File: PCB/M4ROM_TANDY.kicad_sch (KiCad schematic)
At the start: 7 parts, among them J1 Tandy_100_102_200_option_rom, J2 4ROM_prog_female, SW1 CUS-14TB, U1 29F010

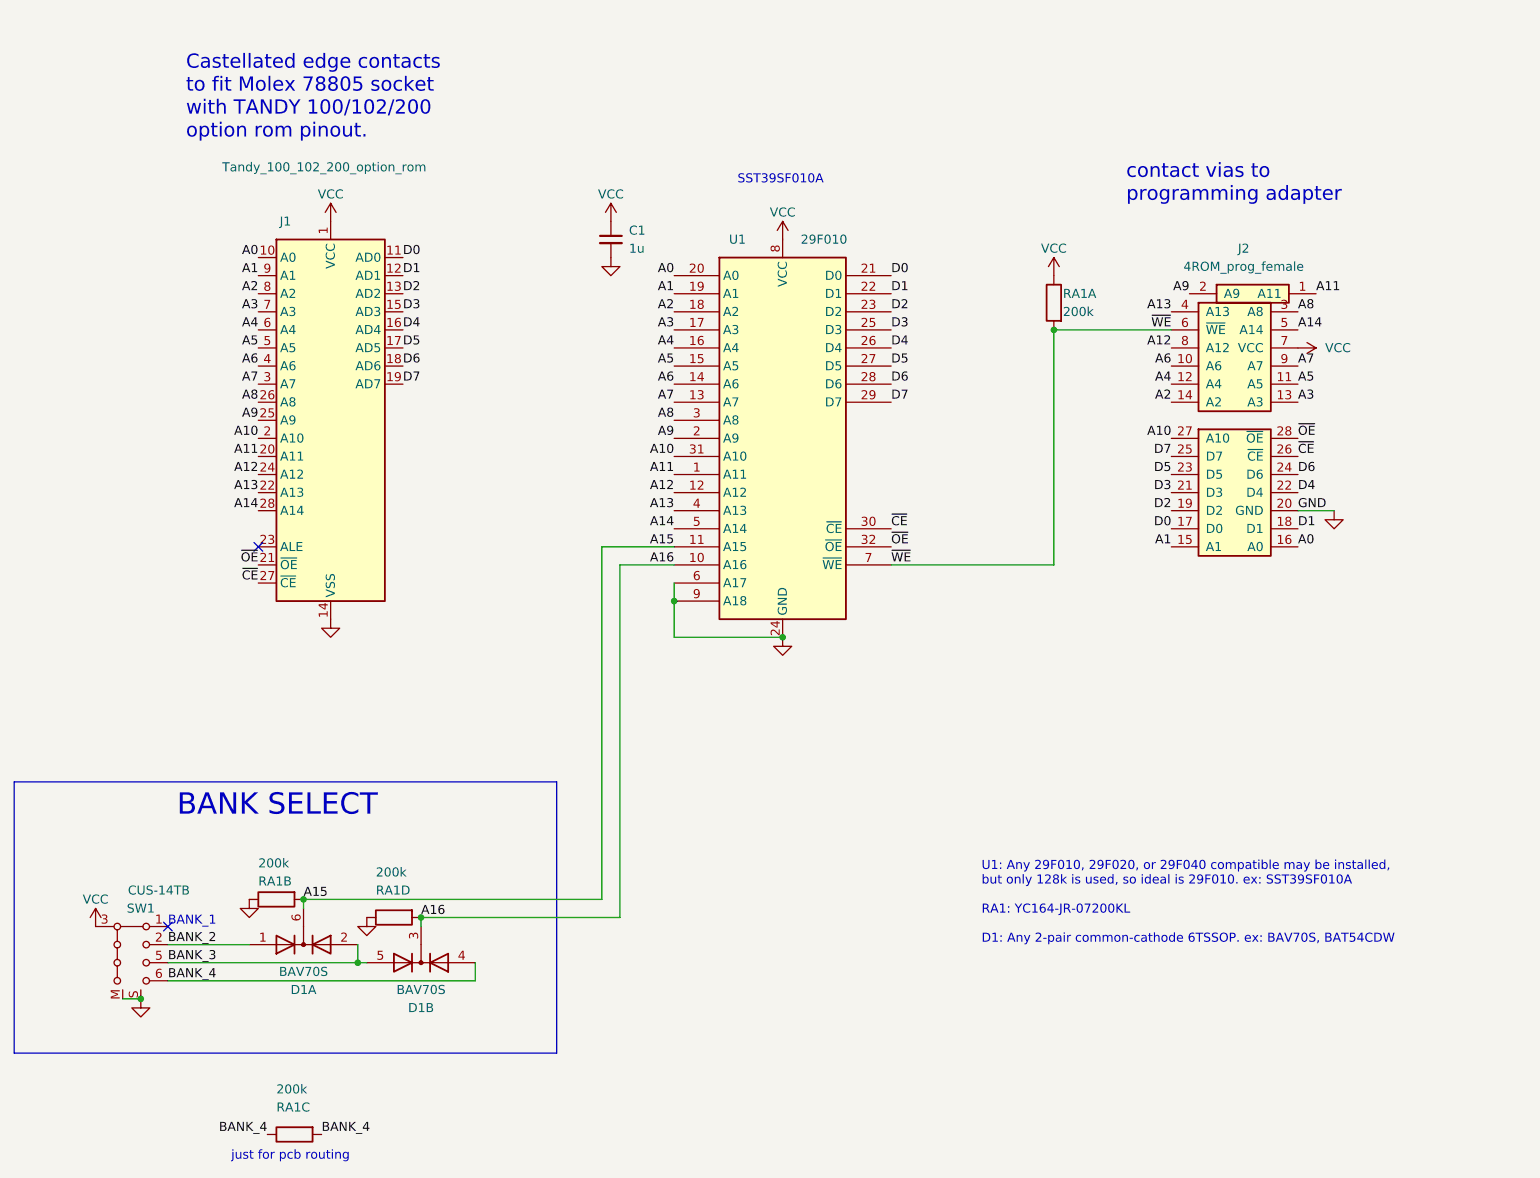
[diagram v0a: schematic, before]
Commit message: MPN boms, centroids, and chip unavailability notes
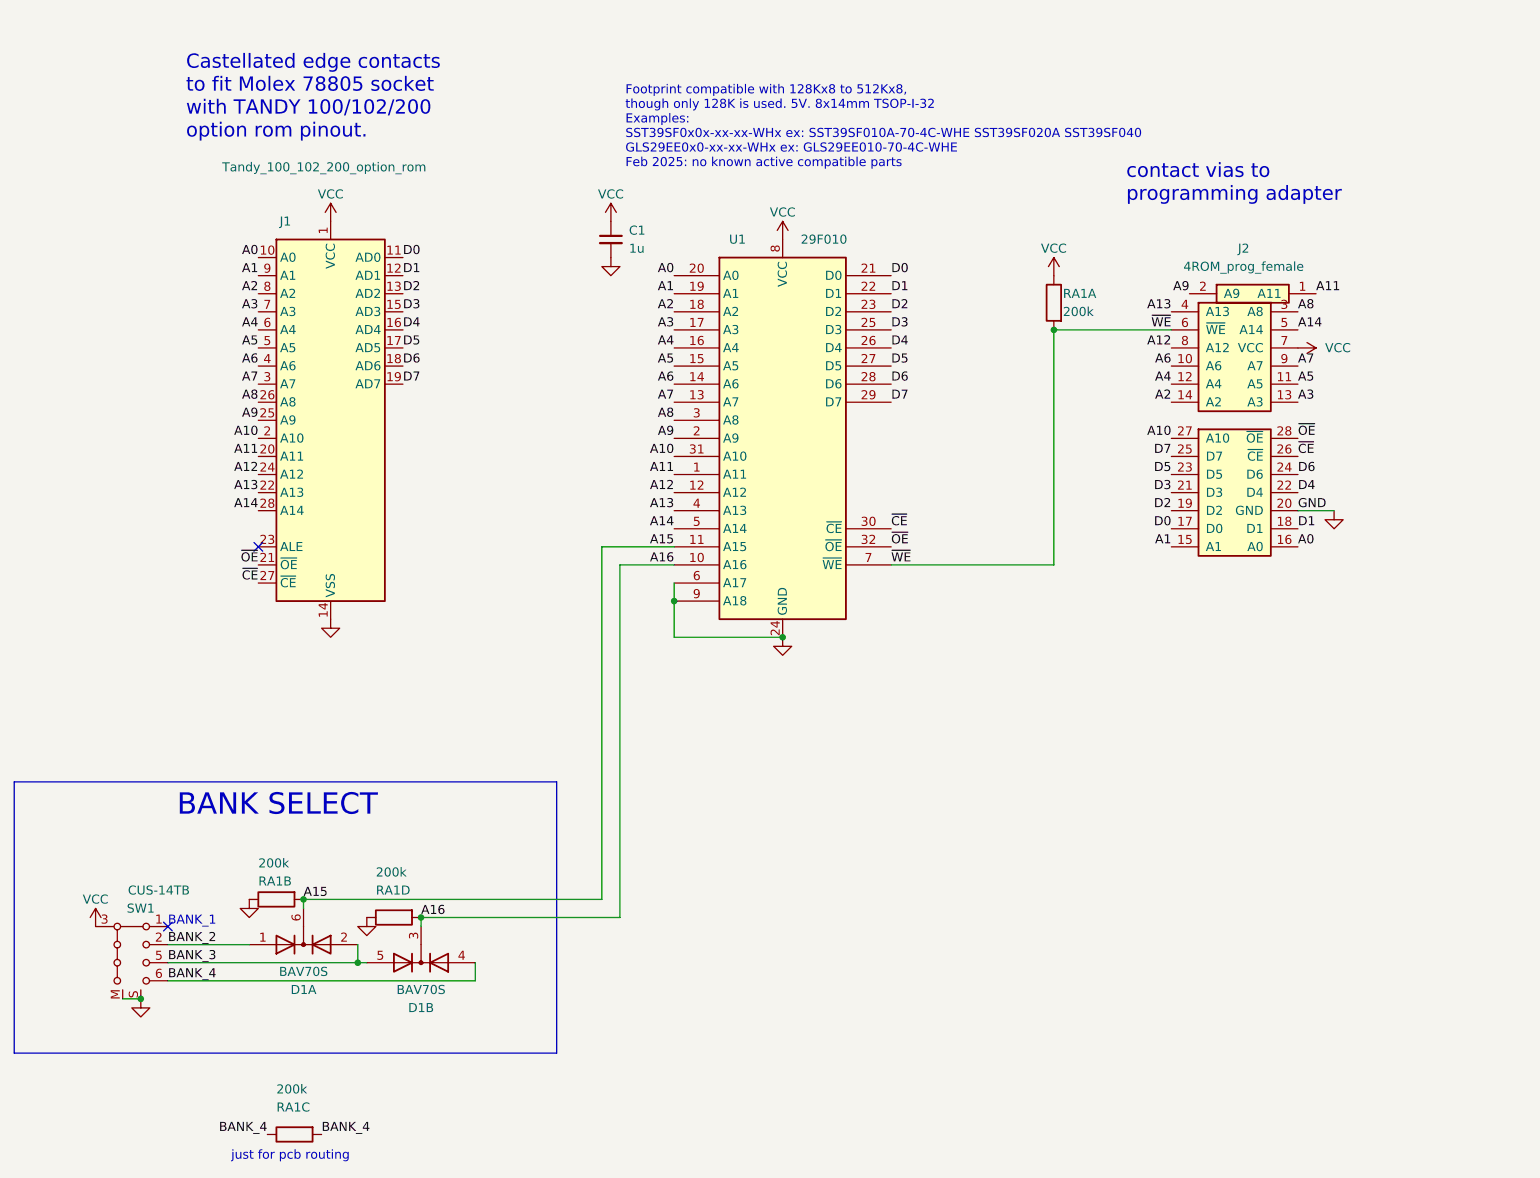
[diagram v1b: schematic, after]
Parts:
- C1: MPN (none) -> CL21B105KBFNNNE
- D1: MPN (none) -> BAV70S,115
- J1, J2: now left out of the parts list
- RA1: MPN (none) -> YC164-JR-07200KL
- SW1: MPN (none) -> CUS-14TB
- U1: MPN (none) -> SST39SF010A-70-4C-WHE
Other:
- note added: "Footprint compatible with 128Kx8 to 512Kx8, though only 128K is used. 5V. 8x14mm TSOP-I-32 Examples: SST39SF0x0x-xx-xx-WHx ex: SST39SF010A-70-4C-WHE SST39SF020A SST39SF040 GLS29EE0x0-xx-xx-WHx ex: GLS29EE010-70-4C-WHE Feb 2025: no known active compatible parts"
- note removed: "SST39SF010A"
- note removed: "U1: Any 29F010, 29F020, or 29F040 compatible may be installed, but only 128k is used, so ideal is 29F010. ex: SST39SF010A RA1: YC164-JR-07200KL D1: Any 2-pair common-cathode 6TSSOP. ex: BAV70S, BAT54CDW"
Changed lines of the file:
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@@
 	(title_block
 		(title "M4ROM TANDY")
-		(date "2023-12-31")
-		(rev "008")
+		(date "2025-02-21")
+		(rev "009")
 		(company "Brian K. White b.kenyon.w@gmail.com")
 		(comment 1 "CC-BY-SA")
@@
 		)
 	)
-	(text "U1: Any 29F010, 29F020, or 29F040 compatible may be installed,\nbut only 128k is used, so ideal is 29F010. ex: SST39SF010A\n\nRA1: YC164-JR-07200KL\n\nD1: Any 2-pair common-cathode 6TSSOP. ex: BAV70S, BAT54CDW\n"
-		(exclude_from_sim no)
-		(at 180.34 162.56 0)
-		(effects
-			(font
-				(size 1.27 1.27)
-			)
-			(justify left bottom)
-		)
-	)
 	(text "BANK SELECT"
 		(exclude_from_sim no)
@@
 		)
 	)
-	(text "SST39SF010A"
+	(text "Footprint compatible with 128Kx8 to 512Kx8,\nthough only 128K is used. 5V. 8x14mm TSOP-I-32\nExamples:\nSST39SF0x0x-xx-xx-WHx ex: SST39SF010A-70-4C-WHE SST39SF020A SST39SF040\nGLS29EE0x0-xx-xx-WHx ex: GLS29EE010-70-4C-WHE\nFeb 2025: no known active compatible parts\n"
 		(exclude_from_sim no)
-		(at 146.05 55.88 0)
+		(at 130.302 53.594 0)
 		(effects
 			(font
@@
 			)
 		)
-		(property "Description" ""
+		(property "Description" "NOR Flash Parallel 5V 128K-512Kx8 TSOP-32"
+			(at 152.4 88.9 0)
+			(effects
+				(font
+					(size 1.27 1.27)
+				)
+				(hide yes)
+			)
+		)
+		(property "MPN" "SST39SF010A-70-4C-WHE"
 			(at 152.4 88.9 0)
 			(effects
@@
 		(unit 1)
 		(exclude_from_sim no)
-		(in_bom yes)
+		(in_bom no)
 		(on_board yes)
 		(dnp no)
@@
 			)
 		)
-		(property "Datasheet" "http://www.vishay.com/docs/31509/csc.pdf"
+		(property "Datasheet" "datasheets/YC164.pdf"
 			(at 97.79 158.75 90)
 			(effects
@@
 			)
 		)
-		(property "Description" ""
+		(property "Description" "RES ARRAY 4 x 200K isolated 1206 4x0612 convex"
 			(at 97.79 158.75 0)
+			(effects
+				(font
+					(size 1.27 1.27)
+				)
+				(hide yes)
+			)
+		)
+		(property "MPN" "YC164-JR-07200KL"
+			(at 97.79 158.75 90)
 			(effects
 				(font
@@
 			)
 		)
-		(property "Datasheet" "datasheet/BAV70S.pdf"
+		(property "Datasheet" "datasheets/BAV70S.pdf"
 			(at 101.6 165.1 0)
 			(effects
@@
 			)
 		)
-		(property "Description" ""
+		(property "Description" "BAV70S 100V 250mA high-speed switching diodes, dual common cathode, SOT-363"
+			(at 101.6 165.1 0)
+			(effects
+				(font
+					(size 1.27 1.27)
+				)
+				(hide yes)
+			)
+		)
+		(property "MPN" "BAV70S,115"
 			(at 101.6 165.1 0)
 			(effects
@@
 			)
 		)
-		(property "Datasheet" "~"
+		(property "Datasheet" "datasheets/cus.pdf"
 			(at 60.96 163.83 0)
 			(effects
@@
 			)
 		)
-		(property "Description" ""
+		(property "Description" "CUS-14TB Switch, 4 position, single pole 4 throw, 4 position switch, SP4T"
+			(at 60.96 163.83 0)
+			(effects
+				(font
+					(size 1.27 1.27)
+				)
+				(hide yes)
+			)
+		)
+		(property "MPN" "CUS-14TB"
 			(at 60.96 163.83 0)
 			(effects
@@
 			)
 		)
-		(property "Datasheet" "~"
+		(property "Datasheet" "datasheets/CL21B105KBFNNNE.pdf"
 			(at 128.27 63.5 0)
 			(effects
@@
 			)
 		)
-		(property "Description" ""
+		(property "Description" "CAP CER 1UF 16V+ 0805"
+			(at 128.27 63.5 0)
+			(effects
+				(font
+					(size 1.27 1.27)
+				)
+				(hide yes)
+			)
+		)
+		(property "MPN" "CL21B105KBFNNNE"
 			(at 128.27 63.5 0)
 			(effects
@@
 			)
 		)
-		(property "Datasheet" "http://www.vishay.com/docs/31509/csc.pdf"
+		(property "Datasheet" "datasheets/YC164.pdf"
 			(at 190.5 72.39 90)
 			(effects
@@
 			)
 		)
-		(property "Description" ""
+		(property "Description" "RES ARRAY 4 x 200K isolated 1206 4x0612 convex"
 			(at 190.5 72.39 0)
+			(effects
+				(font
+					(size 1.27 1.27)
+				)
+				(hide yes)
+			)
+		)
+		(property "MPN" "YC164-JR-07200KL"
+			(at 190.5 72.39 90)
 			(effects
 				(font
@@
 			)
 		)
-		(property "Datasheet" "datasheet/BAV70S.pdf"
+		(property "Datasheet" "datasheets/BAV70S.pdf"
 			(at 85.09 162.56 0)
 			(effects
@@
 			)
 		)
-		(property "Description" ""
+		(property "Description" "BAV70S 100V 250mA high-speed switching diodes, dual common cathode, SOT-363"
+			(at 85.09 162.56 0)
+			(effects
+				(font
+					(size 1.27 1.27)
+				)
+				(hide yes)
+			)
+		)
+		(property "MPN" "BAV70S,115"
 			(at 85.09 162.56 0)
 			(effects
@@
 			)
 		)
-		(property "Datasheet" "http://www.vishay.com/docs/31509/csc.pdf"
+		(property "Datasheet" "datasheets/YC164.pdf"
 			(at 83.82 189.23 90)
 			(effects
@@
 			)
 		)
-		(property "Description" ""
+		(property "Description" "RES ARRAY 4 x 200K isolated 1206 4x0612 convex"
 			(at 83.82 189.23 0)
+			(effects
+				(font
+					(size 1.27 1.27)
+				)
+				(hide yes)
+			)
+		)
+		(property "MPN" "YC164-JR-07200KL"
+			(at 83.82 189.23 90)
 			(effects
 				(font
@@
 		(unit 1)
 		(exclude_from_sim no)
-		(in_bom yes)
+		(in_bom no)
 		(on_board yes)
 		(dnp no)
@@
 			)
 		)
-		(property "Datasheet" "http://www.vishay.com/docs/31509/csc.pdf"
+		(property "Datasheet" "datasheets/YC164.pdf"
 			(at 81.28 156.21 90)
 			(effects
@@
 			)
 		)
-		(property "Description" ""
+		(property "Description" "RES ARRAY 4 x 200K isolated 1206 4x0612 convex"
 			(at 81.28 156.21 0)
 			(effects
 				(font
+					(size 1.27 1.27)
+				)
+				(hide yes)
+			)
+		)
+		(property "MPN" "YC164-JR-07200KL"
+			(at 81.28 156.21 90)
+			(effects
+				(font

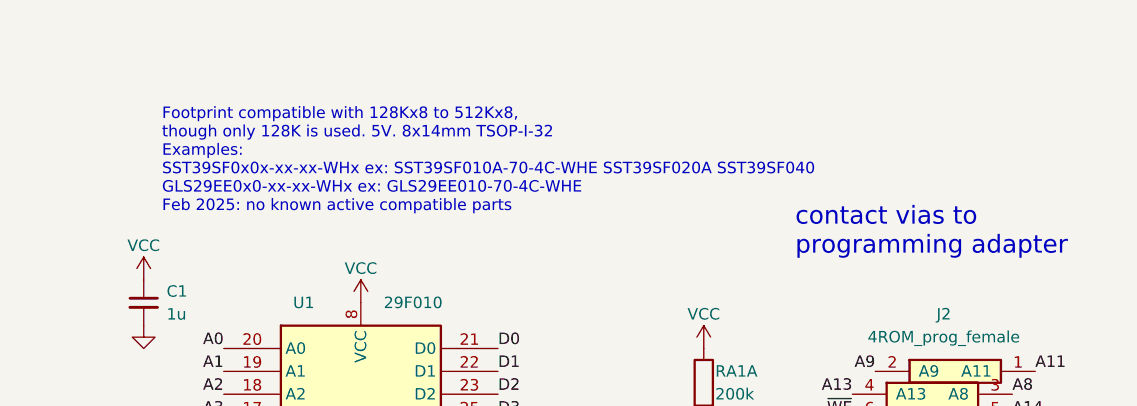
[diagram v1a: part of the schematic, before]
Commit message: new flash part number
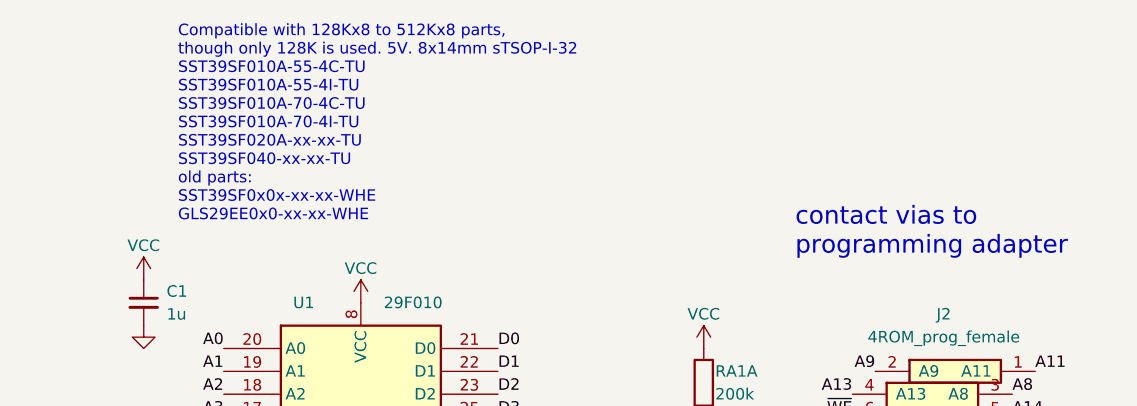
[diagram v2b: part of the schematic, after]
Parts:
- U1: MPN SST39SF010A-70-4C-WHE -> SST39SF010A-70-4C-TU
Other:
- note added: "Compatible with 128Kx8 to 512Kx8 parts, though only 128K is used. 5V. 8x14mm sTSOP-I-32 SST39SF010A-55-4C-TU SST39SF010A-55-4I-TU SST39SF010A-70-4C-TU SST39SF010A-70-4I-TU SST39SF020A-xx-xx-TU SST39SF040-xx-xx-TU old parts: SST39SF0x0x-xx-xx-WHE GLS29EE0x0-xx-xx-WHE"
- note removed: "Footprint compatible with 128Kx8 to 512Kx8, though only 128K is used. 5V. 8x14mm TSOP-I-32 Examples: SST39SF0x0x-xx-xx-WHx ex: SST39SF010A-70-4C-WHE SST39SF020A SST39SF040 GLS29EE0x0-xx-xx-WHx ex: GLS29EE010-70-4C-WHE Feb 2025: no known active compatible parts"
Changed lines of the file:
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@@
 		)
 	)
-	(text "Footprint compatible with 128Kx8 to 512Kx8,\nthough only 128K is used. 5V. 8x14mm TSOP-I-32\nExamples:\nSST39SF0x0x-xx-xx-WHx ex: SST39SF010A-70-4C-WHE SST39SF020A SST39SF040\nGLS29EE0x0-xx-xx-WHx ex: GLS29EE010-70-4C-WHE\nFeb 2025: no known active compatible parts\n"
+	(text "Compatible with 128Kx8 to 512Kx8 parts,\nthough only 128K is used. 5V. 8x14mm sTSOP-I-32\nSST39SF010A-55-4C-TU\nSST39SF010A-55-4I-TU\nSST39SF010A-70-4C-TU\nSST39SF010A-70-4I-TU\nSST39SF020A-xx-xx-TU\nSST39SF040-xx-xx-TU\nold parts:\nSST39SF0x0x-xx-xx-WHE\nGLS29EE0x0-xx-xx-WHE"
 		(exclude_from_sim no)
-		(at 130.302 53.594 0)
+		(at 132.08 54.61 0)
 		(effects
 			(font
@@
 			)
 		)
-		(property "MPN" "SST39SF010A-70-4C-WHE"
+		(property "MPN" "SST39SF010A-70-4C-TU"
 			(at 152.4 88.9 0)
 			(effects
